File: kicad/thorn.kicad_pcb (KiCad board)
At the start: 2 copper layers, 104.8 x 100 mm, 28 parts, among them J1 Conn_01x04, SW1 MX-NoLed-Hotswap, SW10 MX-NoLed-Hotswap, SW11 MX-NoLed-Hotswap, SW12 MX-NoLed-Hotswap, SW13 RotaryEncoder, SW2 MX-NoLed-Hotswap, SW3 MX-NoLed-Hotswap, SW4 MX-NoLed-Hotswap, SW5 MX-NoLed-Hotswap, SW6 MX-NoLed-Hotswap, SW7 MX-NoLed-Hotswap, SW8 MX-NoLed-Hotswap, SW9 MX-NoLed-Hotswap

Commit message: chore: cleaned up directories
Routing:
- net COL2: track 149.0 -> 137.6 mm
- net ROW4: track 128.2 -> 133.9 mm
- net ROW0: track 113.9 -> 117.3 mm
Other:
- outline, holes or cut-outs redrawn

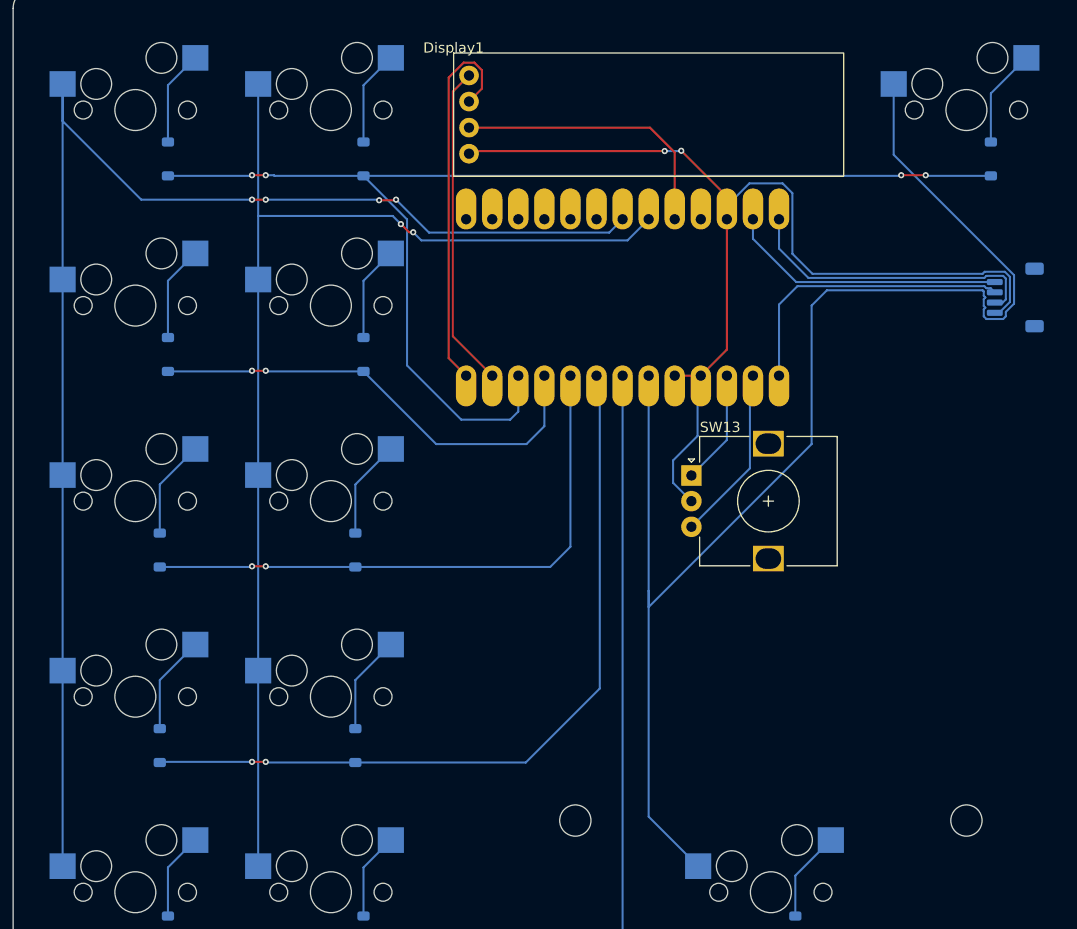
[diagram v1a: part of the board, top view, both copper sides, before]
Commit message: fix: changed pinout for data pins on JST connector
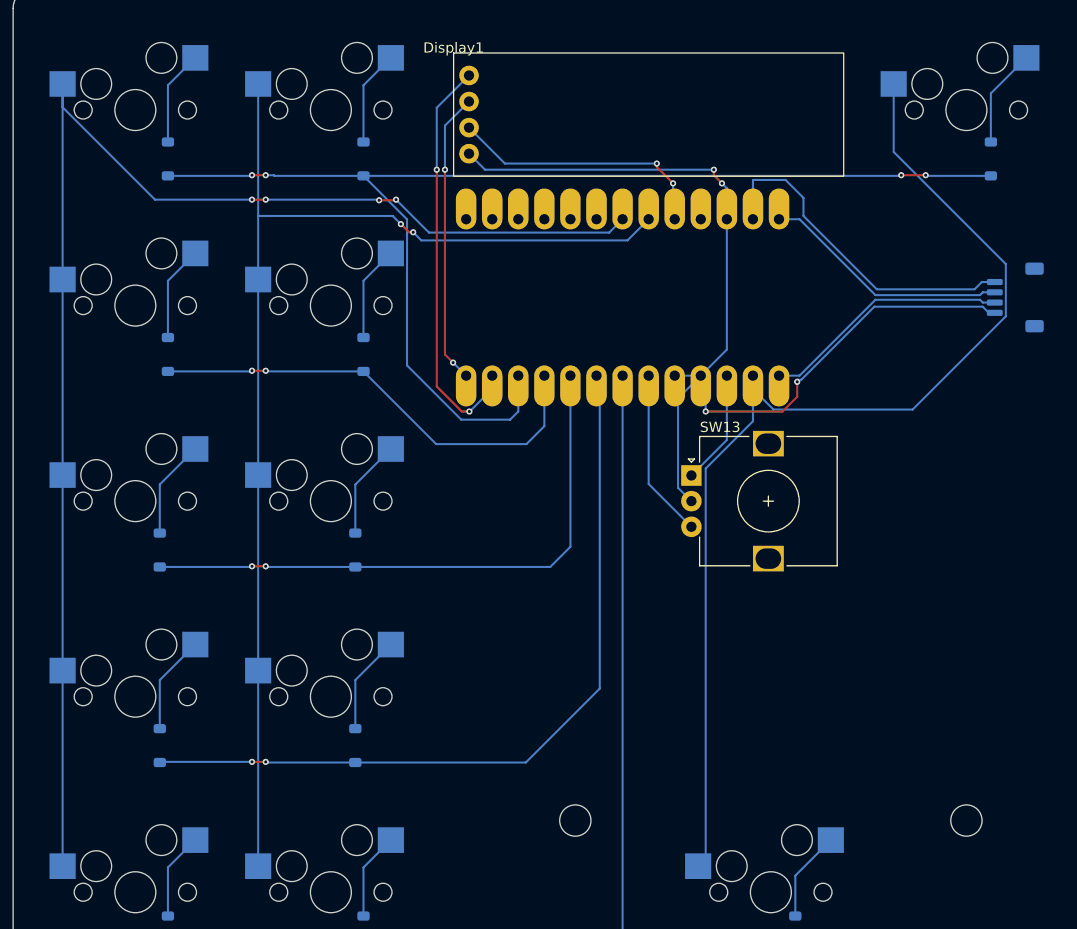
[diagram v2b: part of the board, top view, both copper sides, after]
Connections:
- J1 pad 2: D+ -> D-
- J1 pad 3: D- -> D+
- U1 pad 2: EC2 -> COL2
- U1 pad 6: COL2 -> EC2
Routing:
- net COL2: track 137.6 -> 107.7 mm
- net SCL: track 37.5 -> 28.5 mm, vias 0 -> 2
- net SDA: track 31.5 -> 40.2 mm, vias 0 -> 2
- net RAW: track 27.2 -> 33.1 mm
- net D-: track 29.6 -> 24.2 mm
- net D+: track 28.9 -> 24.2 mm
- net GND: track 103.8 -> 99.6 mm, vias 2 -> 4
- net +3V3: track 27.5 -> 25.9 mm, vias 0 -> 2
- net COL0: track 139.4 -> 138.7 mm
- net EC2: track 17.2 -> 16.4 mm

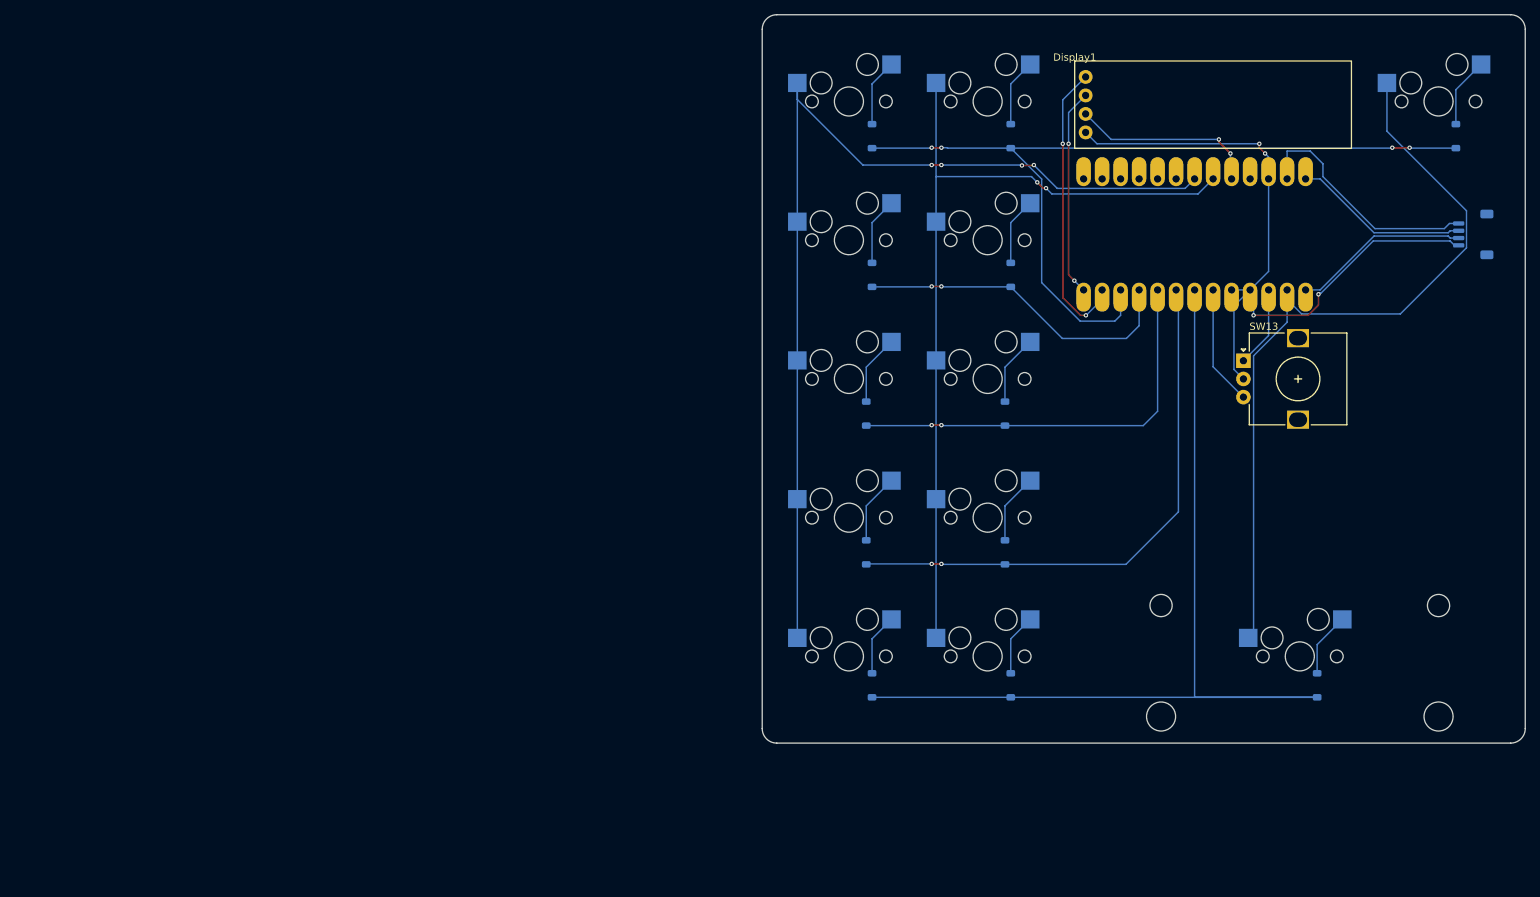
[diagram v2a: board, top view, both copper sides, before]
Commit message: feat: change design to implement rp2040
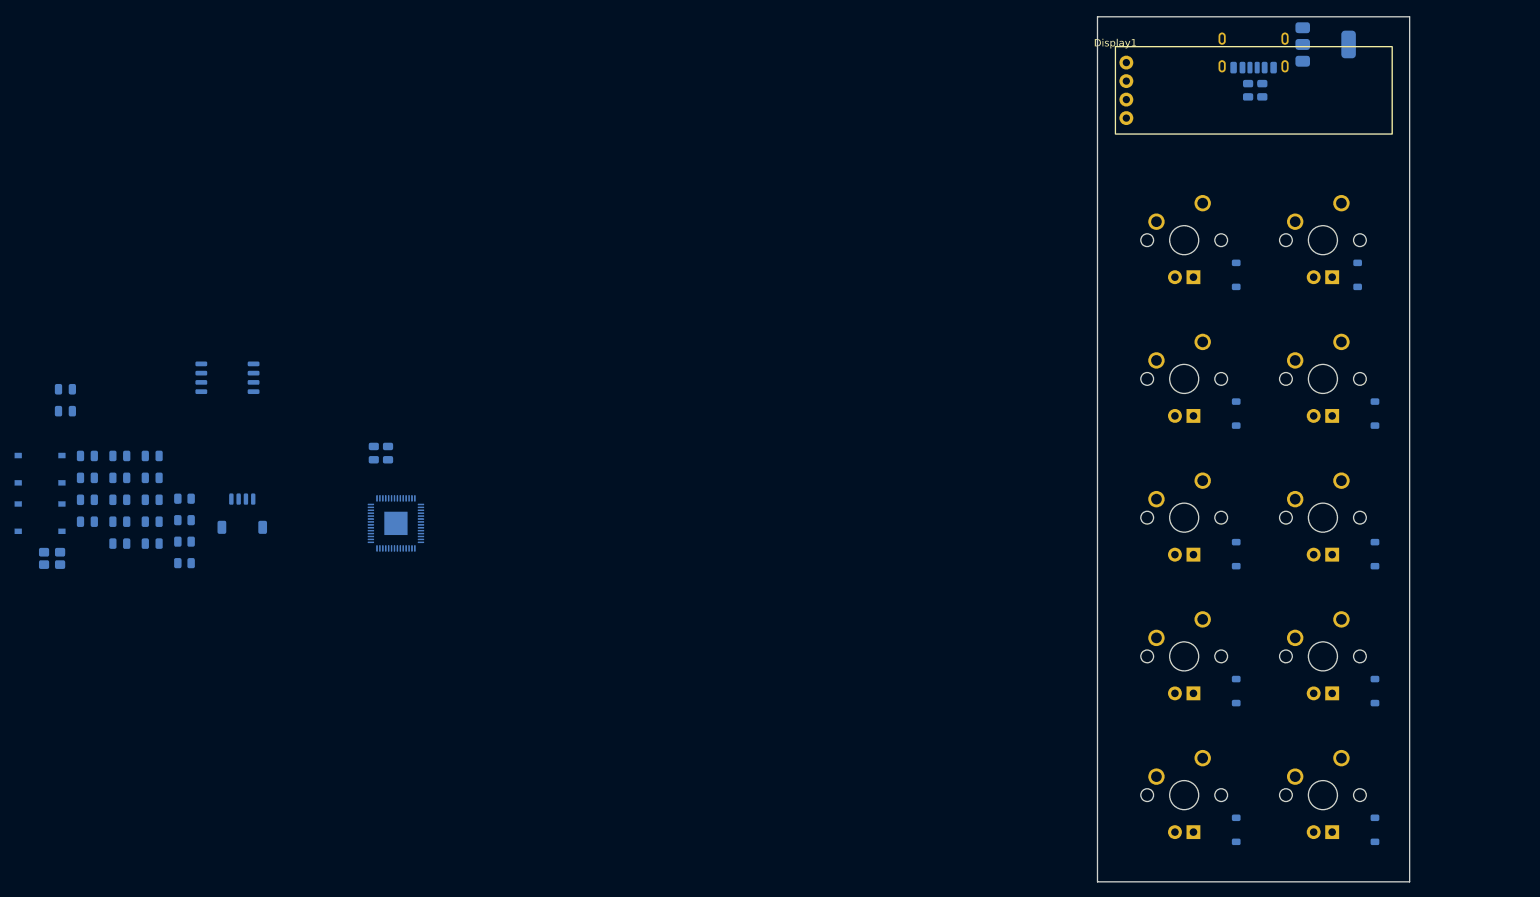
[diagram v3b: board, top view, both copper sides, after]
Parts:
- removed D11, D12: SOD-123, Diode_SMD:D_SOD-123
- removed SW1, SW10, SW2, SW3, SW4, SW5, SW6, SW7, SW8, SW9: MX-NoLed-Hotswap, MX_Only:MXOnly-1U-Hotswap
- removed SW13: RotaryEncoder, Rotary_Encoder:RotaryEncoder_Alps_EC12E_Vertical_H20mm
- added C1: 10u, Capacitor_SMD:C_0805_2012Metric, B.Cu at (-67.9, 87.1)
- added C10: 100n, Capacitor_SMD:C_0805_2012Metric, B.Cu at (-60.4, 102.3)
- added C11: 100n, Capacitor_SMD:C_0805_2012Metric, B.Cu at (-60.4, 105.3)
- added C12: 100n, Capacitor_SMD:C_0805_2012Metric, B.Cu at (-60.4, 108.3)
- added C13: 100n, Capacitor_SMD:C_0805_2012Metric, B.Cu at (-64.9, 96.3)
- added C14: 100n, Capacitor_SMD:C_0805_2012Metric, B.Cu at (-64.9, 99.3)
- added C15: 15p, Capacitor_SMD:C_0805_2012Metric, B.Cu at (-64.9, 102.3)
- added C16: 15p, Capacitor_SMD:C_0805_2012Metric, B.Cu at (-64.9, 105.3)
- added C2: 10u, Capacitor_SMD:C_0805_2012Metric, B.Cu at (-67.9, 90.2)
- added C3: 100n, Capacitor_SMD:C_0805_2012Metric, B.Cu at (-56.0, 96.3)
- added C4: 100n, Capacitor_SMD:C_0805_2012Metric, B.Cu at (-56.0, 99.3)
- added C5: 1u, Capacitor_SMD:C_0805_2012Metric, B.Cu at (-56.0, 102.3)
- added C6: 100n, Capacitor_SMD:C_0805_2012Metric, B.Cu at (-56.0, 105.3)
- added C7: 100n, Capacitor_SMD:C_0805_2012Metric, B.Cu at (-56.0, 108.3)
- added C8: 100n, Capacitor_SMD:C_0805_2012Metric, B.Cu at (-60.4, 96.3)
- added C9: 100n, Capacitor_SMD:C_0805_2012Metric, B.Cu at (-60.4, 99.3)
- added J2: USB_C_Receptacle_USB2.0_14P, Connector_USB:USB_C_Receptacle_HRO_TYPE-C-31-M-17, B.Cu at (95.2, 39.8)
- added MX1: MX-NoLed, MX_Only:MXOnly-1U, F.Cu at (85.7, 66.7)
- added MX10: MX-NoLed, MX_Only:MXOnly-1U, F.Cu at (104.8, 142.9)
- added MX2: MX-NoLed, MX_Only:MXOnly-1U, F.Cu at (104.8, 66.7)
- added MX3: MX-NoLed, MX_Only:MXOnly-1U, F.Cu at (85.7, 85.7)
- added MX4: MX-NoLed, MX_Only:MXOnly-1U, F.Cu at (104.8, 85.7)
- added MX5: MX-NoLed, MX_Only:MXOnly-1U, F.Cu at (85.7, 104.8)
- added MX6: MX-NoLed, MX_Only:MXOnly-1U, F.Cu at (104.8, 104.8)
- added MX7: MX-NoLed, MX_Only:MXOnly-1U, F.Cu at (85.7, 123.8)
- added MX8: MX-NoLed, MX_Only:MXOnly-1U, F.Cu at (104.8, 123.8)
- added MX9: MX-NoLed, MX_Only:MXOnly-1U, F.Cu at (85.7, 142.9)
- added R1: 5.1k, Resistor_SMD:R_0805_2012Metric, B.Cu at (94.5, 46.1)
- added R2: 5.1k, Resistor_SMD:R_0805_2012Metric, B.Cu at (96.5, 46.1)
- added R3: 27.4, Resistor_SMD:R_0805_2012Metric, B.Cu at (-25.6, 95.9)
- added R4: 27.4, Resistor_SMD:R_0805_2012Metric, B.Cu at (-23.6, 95.9)
- added R5: 1k, Resistor_SMD:R_0805_2012Metric, B.Cu at (-51.6, 102.2)
- added R6: DNF, Resistor_SMD:R_0805_2012Metric, B.Cu at (-51.6, 105.1)
- added R7: 1k, Resistor_SMD:R_0805_2012Metric, B.Cu at (-51.6, 108.1)
- added R8: 5.1k, Resistor_SMD:R_0805_2012Metric, B.Cu at (-51.6, 111.0)
- added U2: NCP1117-3.3_SOT223, Package_TO_SOT_SMD:SOT-223-3_TabPin2, B.Cu at (105.2, 39.8)
- added U3: W25Q128JVS, Package_SO:SOIC-8_5.3x5.3mm_P1.27mm, B.Cu at (-45.6, 85.6)
- added Y1: Crystal_GND24, Crystal:Crystal_SMD_3225-4Pin_3.2x2.5mm, B.Cu at (-69.7, 110.4)
- SW11: value MX-NoLed-Hotswap -> SW_Push; footprint MX_Only:MXOnly-1U-Hotswap -> Button_Switch_SMD:SW_Push_1P1T_XKB_TS-1187A; moved to B.Cu
- SW12: value MX-NoLed-Hotswap -> SW_Push; footprint MX_Only:MXOnly-3U-Hotswap -> Button_Switch_SMD:SW_Push_1P1T_XKB_TS-1187A; moved to B.Cu
- U1: value ~ -> RP2040; footprint Pro_Micro_Library:KB2040_SMD -> Package_DFN_QFN:QFN-56-1EP_7x7mm_P0.4mm_EP3.2x3.2mm
- moved SW11 198.6 mm to (-71.4, 98.1), turned to 180 degrees
- moved SW12 174.0 mm to (-71.4, 104.8), turned to 180 degrees
- moved J1 173.3 mm to (-43.6, 104.2), turned to 180 degrees
- moved U1 116.6 mm to (-22.5, 105.6), turned to 180 degrees
- moved D5 54.3 mm to (92.9, 109.8)
- moved D6 54.3 mm to (111.9, 109.8)
- moved D7 54.3 mm to (92.9, 128.6)
- moved D8 54.3 mm to (111.9, 128.6)
- moved D9 53.8 mm to (92.9, 147.6)
- moved D10 53.8 mm to (111.9, 147.6)
- moved D1 53.5 mm to (92.9, 71.4)
- moved D3 53.5 mm to (92.9, 90.5)
- moved D4 53.5 mm to (111.9, 90.5)
- moved D2 51.3 mm to (109.5, 71.4)
- moved Display1 5.92 mm to (76.3, 40.1)
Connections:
- D4 pad 2: Net-(D4-A) -> unconnected-(D4-A-Pad2)
- SW11 pad 1: COL2 -> GND
- SW11 pad 2: Net-(D11-A) -> BOOT
- SW12 pad 1: COL2 -> GND
- SW12 pad 2: Net-(D12-A) -> RESET
- U1 pad 1: D+ -> +3V3
- U1 pad 10: ROW1 -> +3V3
- U1 pad 11: ROW0 -> unconnected-(U1-GPIO8-Pad11)
- U1 pad 12: SDA -> unconnected-(U1-GPIO9-Pad12)
- U1 pad 13: SCL -> unconnected-(U1-GPIO10-Pad13)
- U1 pad 2: COL2 -> unconnected-(U1-GPIO0-Pad2)
- U1 pad 20: COL0 -> unconnected-(U1-XIN-Pad20)
- U1 pad 21: COL1 -> unconnected-(U1-XOUT-Pad21)
- U1 pad 23: unconnected-(U1-RESET-Pad23) -> +3V3
- U1 pad 24: GND -> unconnected-(U1-SWCLK-Pad24)
- U1 pad 25: RAW -> unconnected-(U1-SWDIO-Pad25)
- U1 pad 26: D- -> unconnected-(U1-RUN-Pad26)
- U1 pad 3: EC1 -> unconnected-(U1-GPIO1-Pad3)
- U1 pad 4: GND -> unconnected-(U1-GPIO2-Pad4)
- U1 pad 5: GND -> unconnected-(U1-GPIO3-Pad5)
- U1 pad 6: EC2 -> unconnected-(U1-GPIO4-Pad6)
- U1 pad 7: ROW4 -> unconnected-(U1-GPIO5-Pad7)
- U1 pad 8: ROW3 -> unconnected-(U1-GPIO6-Pad8)
- U1 pad 9: ROW2 -> unconnected-(U1-GPIO7-Pad9)
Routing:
- net COL0: track 138.7 -> 0.00 mm, vias 4 -> 0
- net ROW4: track 133.9 -> 0.00 mm
- net ROW0: track 117.3 -> 0.00 mm, vias 4 -> 0
- net COL1: track 116.1 -> 0.00 mm, vias 2 -> 0
- net COL2: track 107.7 -> 0.00 mm
- net GND: track 99.6 -> 0.00 mm, vias 4 -> 0
- net ROW3: track 76.5 -> 0.00 mm, vias 2 -> 0
- net ROW2: track 57.5 -> 0.00 mm, vias 2 -> 0
- net ROW1: track 45.3 -> 0.00 mm, vias 2 -> 0
- net SDA: track 40.2 -> 0.00 mm, vias 2 -> 0
- net RAW: track 33.1 -> 0.00 mm
- net SCL: track 28.5 -> 0.00 mm, vias 2 -> 0
- net +3V3: track 25.9 -> 0.00 mm, vias 2 -> 0
- net D-: track 24.2 -> 0.00 mm
- net D+: track 24.2 -> 0.00 mm
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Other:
- board size 104.8 x 100 mm -> 42.9 x 118.8 mm

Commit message: chore: cleaned up schematic
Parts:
- C1, C10, C11, C12, C13, C14, C15, C16, C2, C3, C4, C5, C7, C8, C9, J1, J2, R1, R2, R3, R4, R5, R6, R7, R8, SW11, SW12, U1, U2, U3, Y1: moved to F.Cu
- C6: value 100n -> 1u; moved to F.Cu
- MX1, MX10, MX2, MX3, MX4, MX5, MX6, MX7, MX8, MX9: footprint MX_Only:MXOnly-1U -> MX_Only:MXOnly-1U-NoLED
- moved U2 225.7 mm to (-103.5, 125.8)
- moved J2 212.4 mm to (-102.6, 117.1)
- moved R2 202.2 mm to (-90.1, 124.2), turned to 0 degrees
- moved R1 199.3 mm to (-90.1, 121.2), turned to 0 degrees
- moved R4 83.0 mm to (-106.2, 88.0), turned to 0 degrees
- moved R3 81.4 mm to (-106.2, 85.0), turned to 0 degrees
- moved U1 65.0 mm to (-87.5, 105.2), turned to 0 degrees
- moved R5 55.8 mm to (-106.2, 91.0), turned to 0 degrees
- moved R6 55.8 mm to (-106.2, 93.9), turned to 0 degrees
- moved R7 55.8 mm to (-106.2, 96.8), turned to 0 degrees
- moved R8 55.8 mm to (-106.2, 99.8), turned to 0 degrees
- moved U3 55.7 mm to (-98.9, 102.2), turned to 0 degrees
- moved J1 50.1 mm to (-92.3, 115.9), turned to 0 degrees
- moved C3 47.2 mm to (-101.8, 85.1), turned to 0 degrees
- moved C4 47.2 mm to (-101.8, 88.1), turned to 0 degrees
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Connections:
- D4 pad 2: unconnected-(D4-A-Pad2) -> Net-(D4-A)
- MX4 pad 2: unconnected-(MX4-Pad2) -> Net-(D4-A)
- U1 pad 19: unconnected-(U1-TESTEN-Pad19) -> GND
- U1 pad 20: unconnected-(U1-XIN-Pad20) -> XIN
- U1 pad 21: unconnected-(U1-XOUT-Pad21) -> XOUT
- U1 pad 24: unconnected-(U1-SWCLK-Pad24) -> SWCLK
- U1 pad 25: unconnected-(U1-SWDIO-Pad25) -> SWDIO
- U1 pad 26: unconnected-(U1-RUN-Pad26) -> RESET
- U1 pad 30: unconnected-(U1-GPIO19-Pad30) -> ROW0
- U1 pad 31: unconnected-(U1-GPIO20-Pad31) -> ROW1
- U1 pad 32: unconnected-(U1-GPIO21-Pad32) -> ROW2
- U1 pad 34: unconnected-(U1-GPIO22-Pad34) -> ROW3
- U1 pad 35: unconnected-(U1-GPIO23-Pad35) -> ROW4
- U1 pad 36: unconnected-(U1-GPIO24-Pad36) -> COL1
- U1 pad 37: unconnected-(U1-GPIO25-Pad37) -> COL0
- U1 pad 51: unconnected-(U1-QSPI_SD3-Pad51) -> QSPI_SD3
- U1 pad 52: unconnected-(U1-QSPI_SCLK-Pad52) -> QSPI_SCLK
- U1 pad 53: unconnected-(U1-QSPI_SD0-Pad53) -> QSPI_SD0
- U1 pad 54: unconnected-(U1-QSPI_SD2-Pad54) -> QSPI_SD2
- U1 pad 55: unconnected-(U1-QSPI_SD1-Pad55) -> QSPI_SD1
- U1 pad 56: unconnected-(U1-~{QSPI_SS}-Pad56) -> QSPI_SS
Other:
- board size 42.9 x 118.8 mm -> 42.9 x 115.5 mm

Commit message: feat: finished preliminary wiring
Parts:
- added J4: Conn_01x07, Connector_FFC-FPC:Molex_200528-0070_1x07-1MP_P1.00mm_Horizontal, F.Cu at (136.9, 98.6)
- added J5: Conn_01x07, Connector_FFC-FPC:Molex_200528-0070_1x07-1MP_P1.00mm_Horizontal, B.Cu at (105.2, 50.5)
- added J6: Conn_01x07, Connector_FFC-FPC:Molex_200528-0070_1x07-1MP_P1.00mm_Horizontal, F.Cu at (136.9, 113.2)
- added J7: Conn_01x07, Connector_FFC-FPC:Molex_200528-0070_1x07-1MP_P1.00mm_Horizontal, B.Cu at (171.4, 52.1)
- added SW1: RotaryEncoder, Rotary_Encoder:RotaryEncoder_Alps_EC12E_Vertical_H20mm, F.Cu at (144.6, 49.8)
- added U4: SRV05-4, Package_TO_SOT_SMD:SOT-23-6, F.Cu at (152.2, 79.3)
- J2: footprint Connector_USB:USB_C_Receptacle_HRO_TYPE-C-31-M-17 -> Connector_USB:USB_C_Receptacle_JAE_DX07S016JA1R1500
- moved R8 269.1 mm to (162.1, 119.5), turned to -90 degrees
- moved U2 266.0 mm to (159.6, 86.8), turned to 180 degrees
- moved C3 265.9 mm to (164.0, 93.4), turned to 90 degrees
- moved C5 263.9 mm to (162.0, 95.0), turned to 90 degrees
- moved C1 262.4 mm to (165.3, 84.9), turned to -90 degrees
- moved C2 262.3 mm to (165.3, 88.5), turned to -90 degrees
- moved C6 261.8 mm to (160.0, 95.0), turned to 90 degrees
- moved R3 261.6 mm to (155.3, 79.5), turned to 90 degrees
- moved R7 259.5 mm to (153.0, 108.3), turned to 180 degrees
- moved C4 259.2 mm to (157.4, 92.9), turned to 90 degrees
- moved J2 258.2 mm to (151.7, 72.5), turned to 180 degrees
- moved C13 257.5 mm to (164.2, 98.5), turned to 90 degrees
- moved C10 257.3 mm to (159.6, 103.2), turned to -90 degrees
- moved J1 257.2 mm to (161.6, 75.0), turned to 135 degrees
- moved R4 255.5 mm to (149.1, 79.5), turned to 90 degrees
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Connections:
- U1 pad 11: unconnected-(U1-GPIO8-Pad11) -> SDA
- U1 pad 12: unconnected-(U1-GPIO9-Pad12) -> EC1
- U1 pad 13: unconnected-(U1-GPIO10-Pad13) -> EC2
- U1 pad 2: unconnected-(U1-GPIO0-Pad2) -> COL0
- U1 pad 3: unconnected-(U1-GPIO1-Pad3) -> COL1
- U1 pad 30: ROW0 -> unconnected-(U1-GPIO19-Pad30)
- U1 pad 31: ROW1 -> unconnected-(U1-GPIO20-Pad31)
- U1 pad 32: ROW2 -> unconnected-(U1-GPIO21-Pad32)
- U1 pad 34: ROW3 -> unconnected-(U1-GPIO22-Pad34)
- U1 pad 35: ROW4 -> unconnected-(U1-GPIO23-Pad35)
- U1 pad 36: COL1 -> unconnected-(U1-GPIO24-Pad36)
- U1 pad 37: COL0 -> unconnected-(U1-GPIO25-Pad37)
- U1 pad 4: unconnected-(U1-GPIO2-Pad4) -> ROW4
- U1 pad 5: unconnected-(U1-GPIO3-Pad5) -> ROW3
- U1 pad 6: unconnected-(U1-GPIO4-Pad6) -> ROW2
- U1 pad 7: unconnected-(U1-GPIO5-Pad7) -> ROW1
- U1 pad 8: unconnected-(U1-GPIO6-Pad8) -> ROW0
- U1 pad 9: unconnected-(U1-GPIO7-Pad9) -> SCL
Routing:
- net GND: track 0.00 -> 208.3 mm, vias 0 -> 2
- net +3V3: track 0.00 -> 140.4 mm, vias 0 -> 2
- net ROW4: track 0.00 -> 120.9 mm, vias 0 -> 2
- net COL0: track 0.00 -> 103.7 mm
- net ROW3: track 0.00 -> 100.9 mm, vias 0 -> 2
- net COL1: track 0.00 -> 96.7 mm
- net ROW2: track 0.00 -> 81.7 mm, vias 0 -> 2
- net ROW1: track 0.00 -> 62.7 mm, vias 0 -> 2
- net EC2: track 0.00 -> 52.3 mm
- net EC1: track 0.00 -> 50.4 mm
- net ROW0: track 0.00 -> 45.9 mm
- net QSPI_SD3: track 0.00 -> 35.5 mm
- net QSPI_SCLK: track 0.00 -> 32.4 mm
- net SDA: track 0.00 -> 32.1 mm
- net BOOT: track 0.00 -> 32.0 mm, vias 0 -> 4
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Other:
- board size 42.9 x 115.5 mm -> 118.2 x 100.8 mm
- board text added: "BOOT"
- board text added: "RESET"
